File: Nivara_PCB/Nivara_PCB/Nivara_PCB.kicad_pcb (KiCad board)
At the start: 4 copper layers, 98.8 x 81.2 mm, 167 parts, among them CN1 ANALOG_IN, CN2 RELAY, J1 AUXILIAR, K1 SRA-24VDC-CL, K2 SRA-24VDC-CL, P1 NPN_IN, P2 PNP_IN, P3 D_IN, P4 RUN/STOP, P5 NPN_OUT, P6 PNP_OUT, P7 RS485, P8 ANALOG_OUT., Q1 IRLML0040, Q2 AO3407A, Q3 IRLML0040, Q4 AO3407A, Q5 IRLML6402TRPBF-JSM, SW1 SKRPACE010, SW2 SKRPACE010, U1 2.54-2*2, U10 GP8201S-TC50-EW, U11 LK1802, U12 LTV-357T, U13 LTV-357T, U14 LTV-357T, U15 LTV-357T, U16 LTV-357T, U17 LTV-357T, U18 LTV-357T, U19 GP8303-TC50-EW, U2 FUENTE IN, U20 FUENTE EX, U3 ESP32-S3-WROOM-1, U4 AP63200WU, U5 RSM3485ECHT_C2992406, U6 LTV-357T, U7 LTV-357T, U8 LTV-357T, U9 LTV-357T

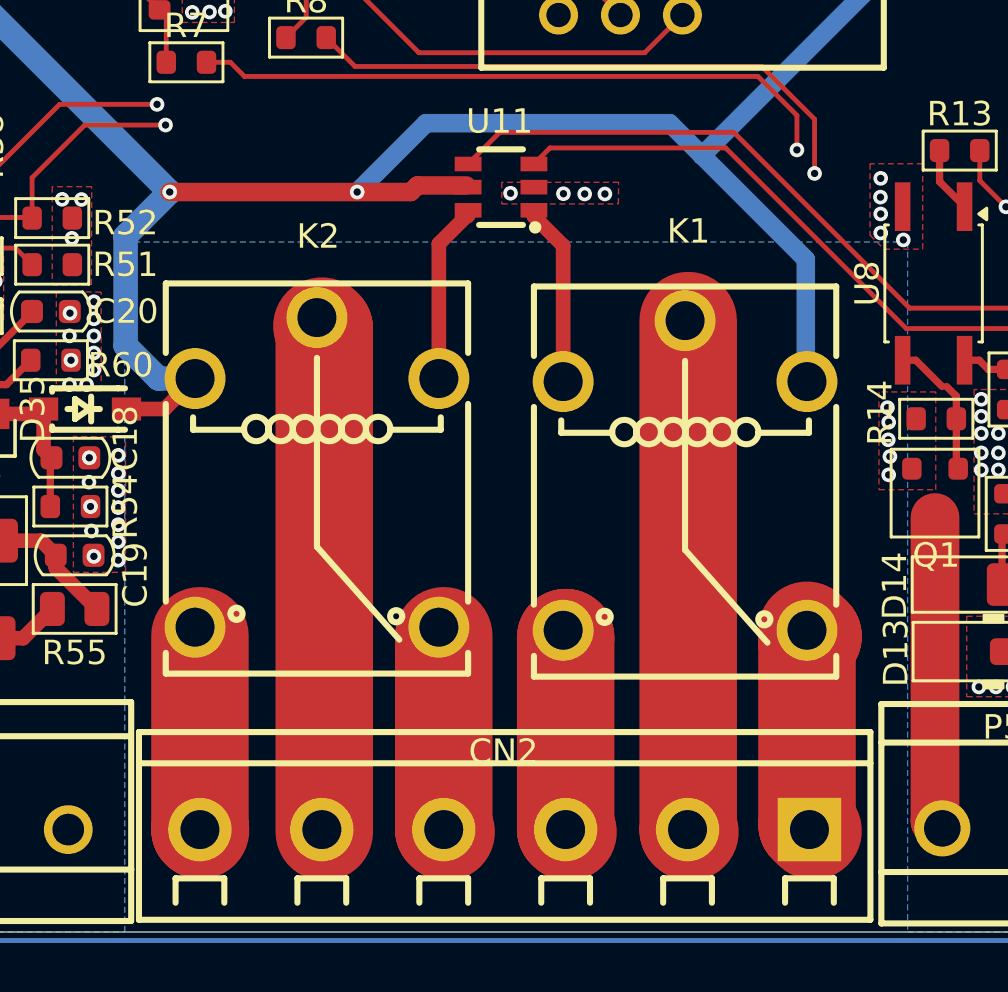
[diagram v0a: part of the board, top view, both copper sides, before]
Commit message: Terminaciones de PCB y esquemáticos.
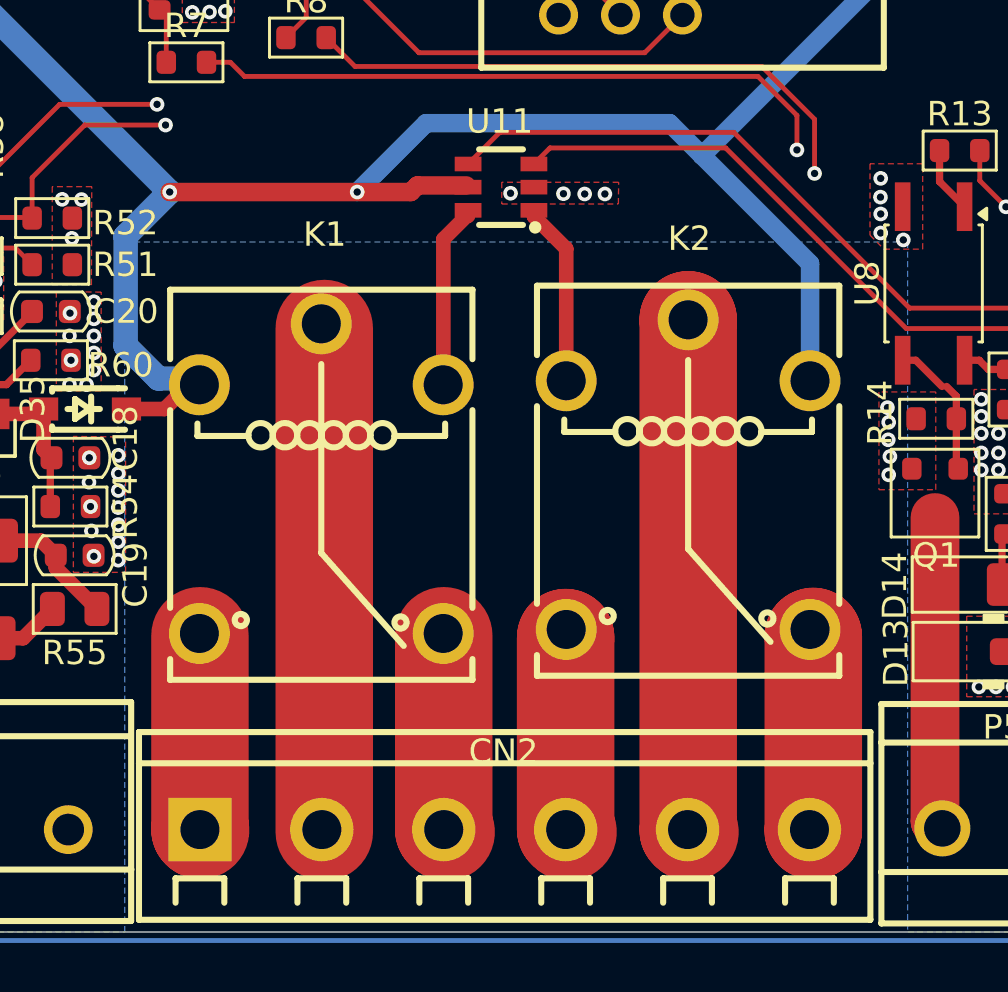
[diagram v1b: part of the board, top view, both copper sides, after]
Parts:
- moved K2 15.2 mm to (214.1, 103.9)
- moved K1 14.9 mm to (199.0, 104.1)
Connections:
- K1 pad 1: /NIVARA_BOARD/RLY_1_NO -> /NIVARA_BOARD/RLY_1_NC
- K1 pad 2: /NIVARA_BOARD/RLY_1_NC -> /NIVARA_BOARD/RLY_1_NO
- K1 pad 3: VCC -> Net-(U11-2C)
- K1 pad 4: Net-(U11-1C) -> VCC
- K2 pad 1: /NIVARA_BOARD/RLY_2_NO -> /NIVARA_BOARD/RLY_2_NC
- K2 pad 2: /NIVARA_BOARD/RLY_2_NC -> /NIVARA_BOARD/RLY_2_NO
- K2 pad 3: Net-(U11-2C) -> VCC
- K2 pad 4: VCC -> Net-(U11-1C)
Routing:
- net /NIVARA_BOARD/RLY_1_NC: track 8.54 -> 7.99 mm

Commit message: Terminaciones de diseño.
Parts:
- removed F1: BSMD1812-150-33V, EasyEDA:F1812
- added U21: ~, EasyEDA:Reseatteble Fuse, F.Cu at (175.6, 50.1)
- moved TP1 2.16 mm to (177.7, 51.7)
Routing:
- net VCC: vias 49 -> 58
- net /VIN: vias 87 -> 96

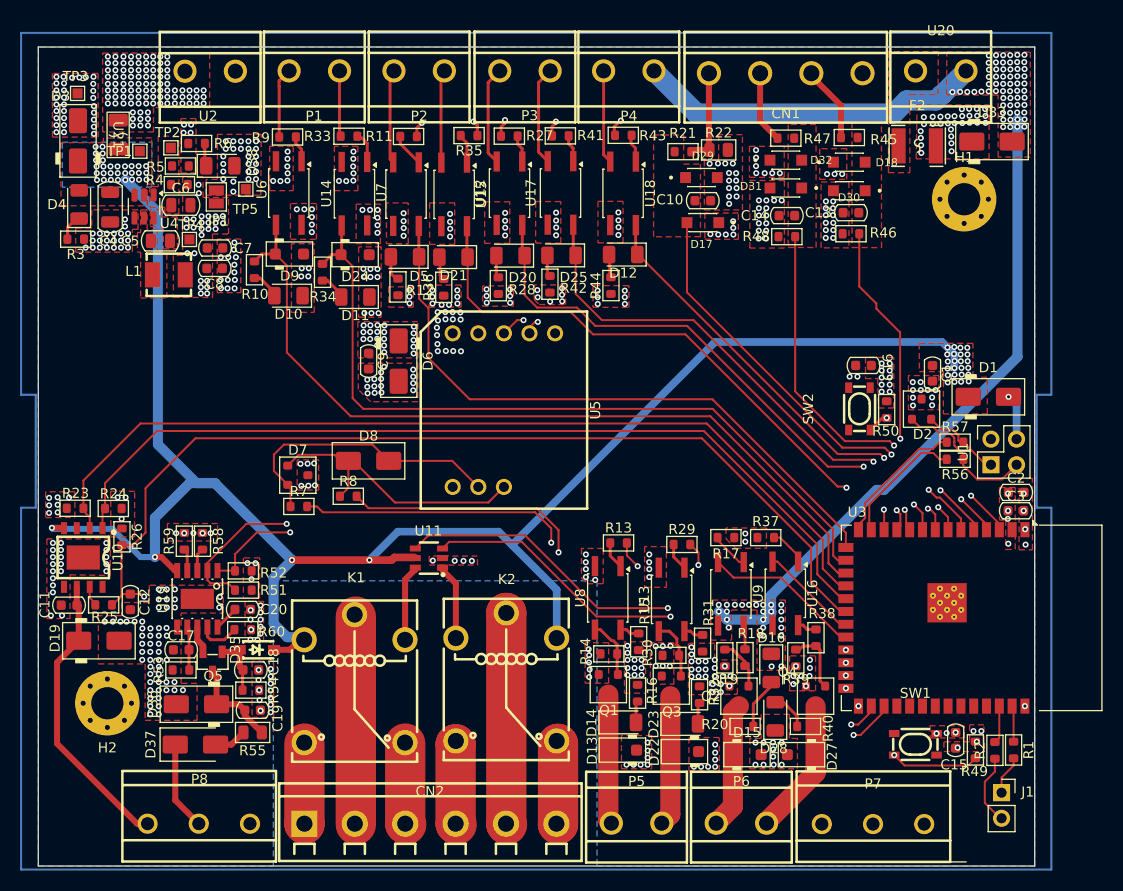
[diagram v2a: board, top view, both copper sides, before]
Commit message: Cambios finales en la comprobación del DRC.
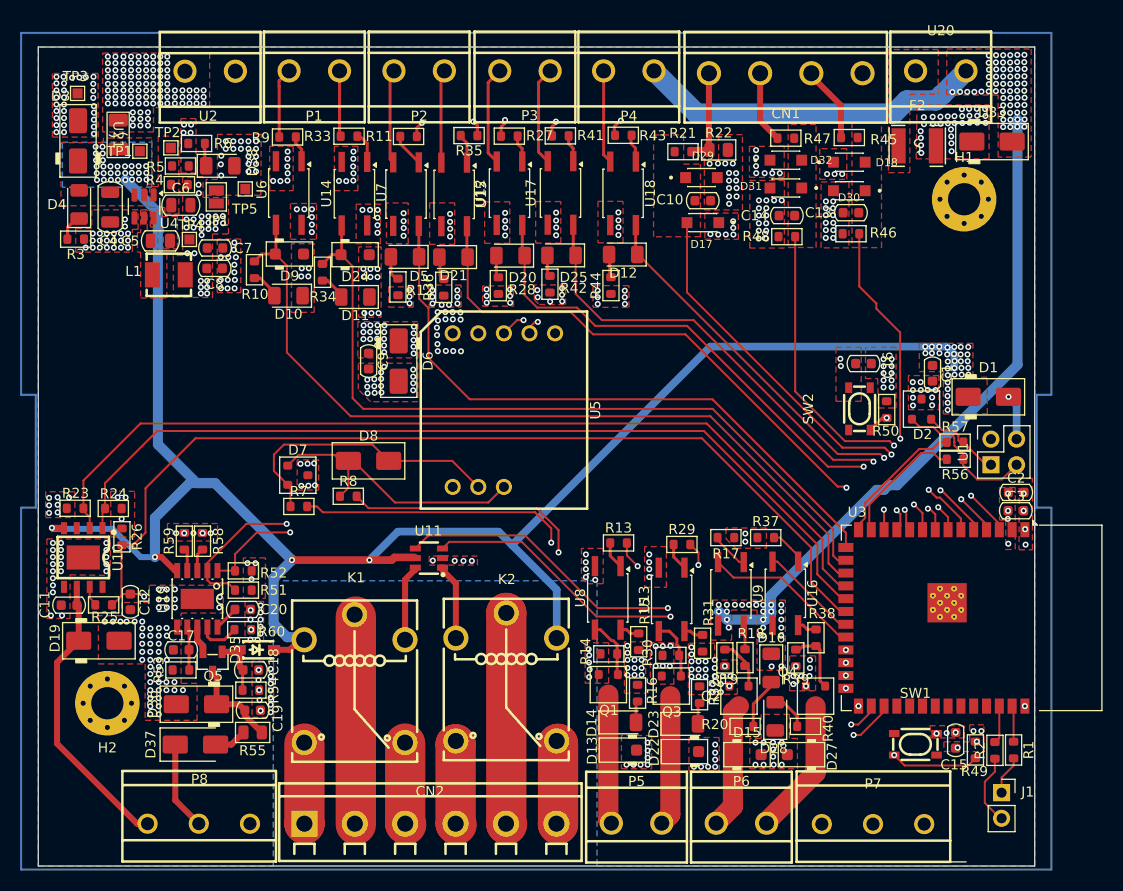
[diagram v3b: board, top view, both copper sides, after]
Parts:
- R11, R33, R35, R9: value 1k -> 2k
- moved C16 0.19 mm to (249.5, 72.8)
- moved TP5 0.06 mm to (188.2, 55.5)
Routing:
- net +3.3V: track 212.7 -> 215.7 mm, vias 149 -> 144
- net VCC: track 179.7 -> 179.3 mm, vias 58 -> 65

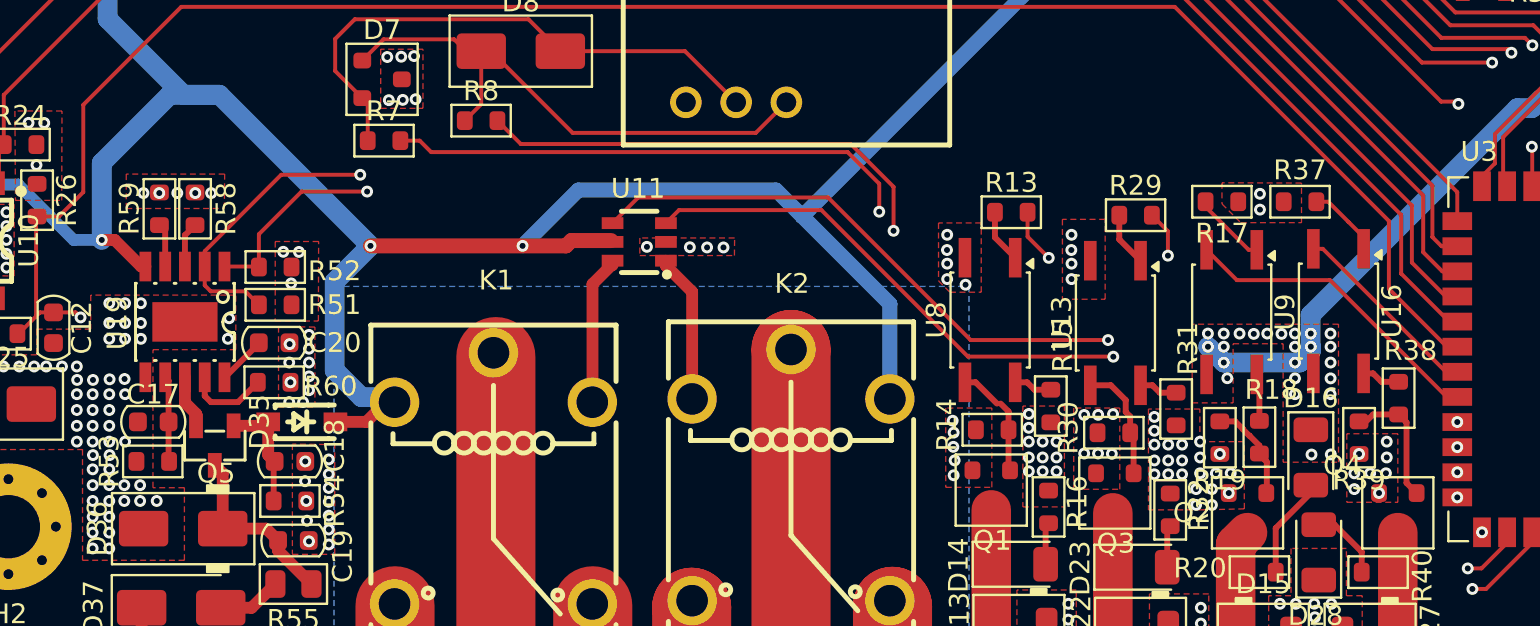
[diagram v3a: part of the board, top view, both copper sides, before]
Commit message: Mejora de distribución de pistas y vías en el PCB.
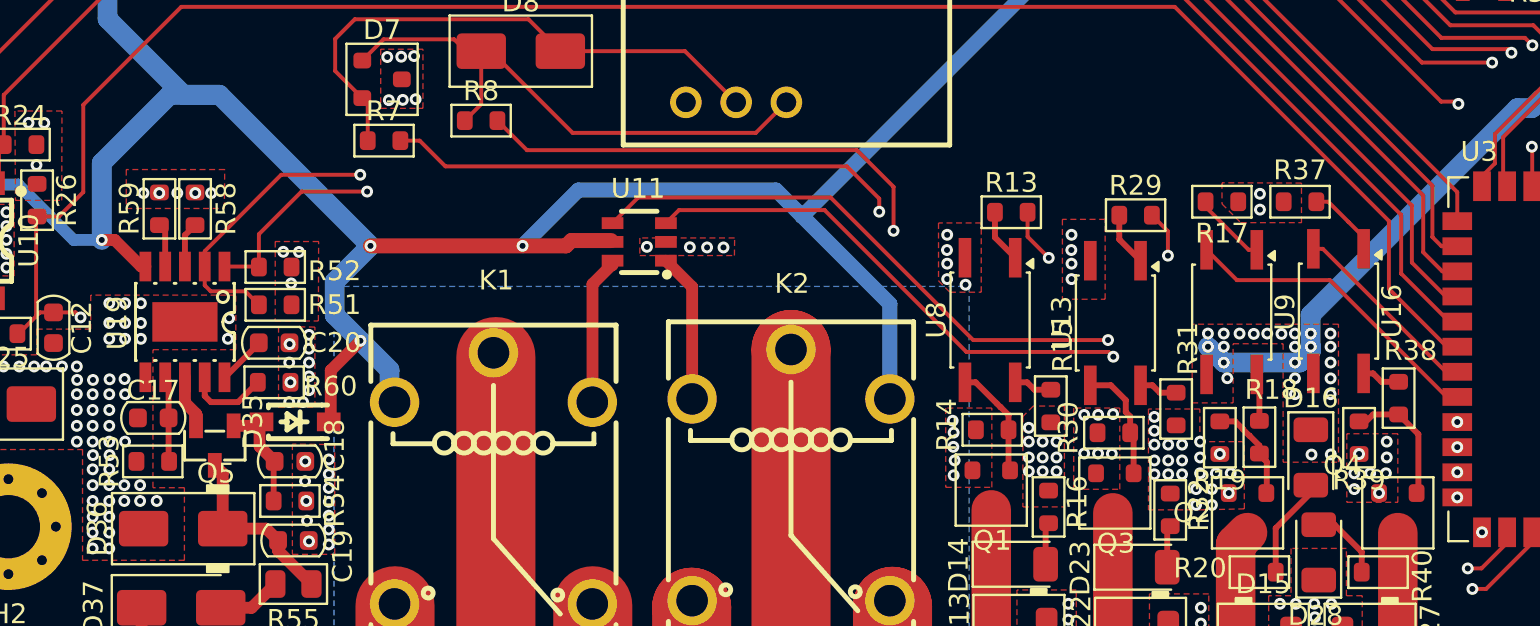
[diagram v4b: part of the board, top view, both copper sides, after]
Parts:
- moved D35 0.34 mm to (189.0, 101.2)
- moved C17 0.20 mm to (181.8, 101.0)
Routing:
- net VCC: track 179.3 -> 179.8 mm, vias 65 -> 66
- net VDD: vias 90 -> 89

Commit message: PCB listo para revisión.
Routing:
- net /NIVARA_BOARD/PNP_IN_1/PNP_OUT: track 63.4 -> 64.1 mm
- net /NIVARA_BOARD/NPN_IN_2/NPN_OUT: track 77.1 -> 77.7 mm
